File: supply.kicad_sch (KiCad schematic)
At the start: 37 parts, among them IC3 TPS259571DSGR, IC4 BQ27427YZFR, IC5 TPD6E001RSERG4, IC7 TPS62291DRVR, IC8 TPS62293DRVR, IC9 MP2722GRH-0000-Z, J4 UJ20-C-V-SMT-TR-68, J6 Conn_01x03

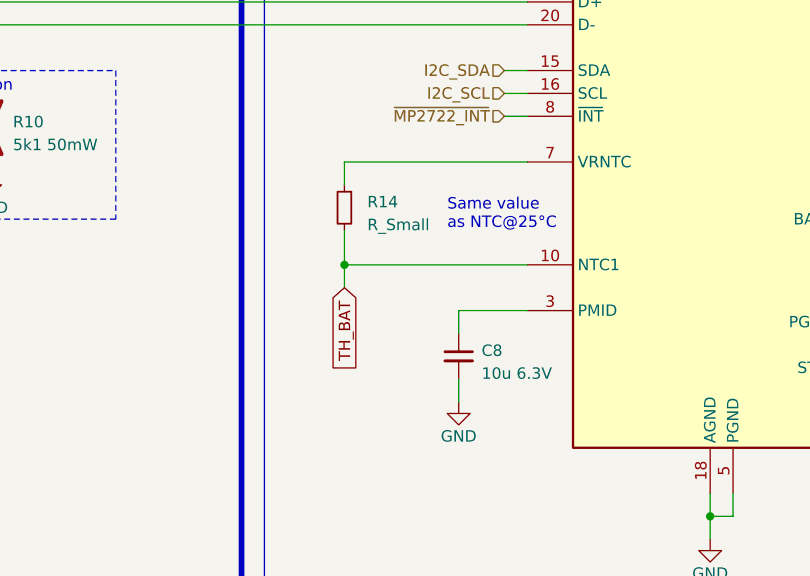
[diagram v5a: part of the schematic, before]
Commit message: added decoupling capacitors to sensors
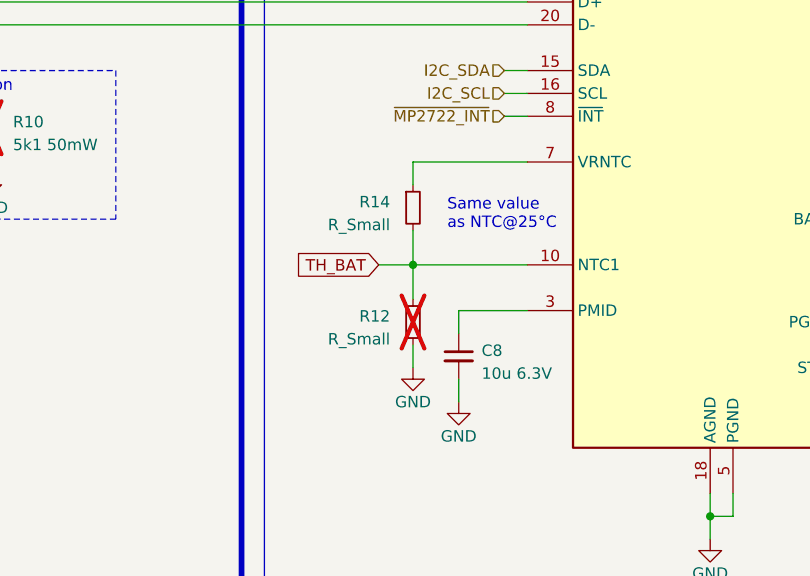
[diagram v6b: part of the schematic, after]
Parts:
- added R12: R_Small, Resistor_SMD:R_0201_0603Metric, symbol Device:R_Small
- R14: footprint (none) -> Resistor_SMD:R_0201_0603Metric
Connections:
- net EP: now also R12.2
- net TH_BAT: now also R12.1
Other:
- moved on the sheet: R14
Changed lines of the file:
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@@
   (junction (at 121.92 137.16) (diameter 0) (color 0 0 0 0)
   )
-  (junction (at 166.37 171.45) (diameter 0) (color 0 0 0 0)
+  (junction (at 173.99 171.45) (diameter 0) (color 0 0 0 0)
   )
   (junction (at 264.16 177.8) (diameter 0) (color 0 0 0 0)
@@
     (stroke (width 0) (type default))
   )
+  (wire (pts (xy 170.18 171.45) (xy 173.99 171.45))
+    (stroke (width 0) (type default))
+  )
   (wire (pts (xy 229.87 172.72) (xy 264.16 172.72))
     (stroke (width 0) (type default))
@@
     (stroke (width 0) (type default))
   )
+  (wire (pts (xy 173.99 180.34) (xy 173.99 182.88))
+    (stroke (width 0) (type default))
+  )
   (wire (pts (xy 209.55 196.85) (xy 209.55 199.39))
     (stroke (width 0) (type default))
@@
     (stroke (width 0) (type default))
   )
-  (wire (pts (xy 166.37 160.02) (xy 166.37 162.56))
+  (wire (pts (xy 173.99 160.02) (xy 173.99 162.56))
     (stroke (width 0) (type default))
   )
@@
     (stroke (width 0) (type default))
   )
-  (wire (pts (xy 166.37 167.64) (xy 166.37 171.45))
+  (wire (pts (xy 173.99 167.64) (xy 173.99 171.45))
     (stroke (width 0) (type default))
   )
@@
     (stroke (width 0) (type default))
   )
+  (wire (pts (xy 173.99 175.26) (xy 173.99 171.45))
+    (stroke (width 0) (type default))
+  )
   (wire (pts (xy 209.55 238.76) (xy 226.06 238.76))
     (stroke (width 0) (type default))
@@
     (stroke (width 0) (type default))
   )
-  (wire (pts (xy 166.37 171.45) (xy 186.69 171.45))
+  (wire (pts (xy 173.99 171.45) (xy 186.69 171.45))
     (stroke (width 0) (type default))
   )
@@
     (stroke (width 0) (type default))
   )
-  (wire (pts (xy 166.37 171.45) (xy 166.37 173.99))
-    (stroke (width 0) (type default))
-  )
   (wire (pts (xy 120.65 77.47) (xy 120.65 81.28))
     (stroke (width 0) (type default))
@@
     (stroke (width 0) (type default))
   )
-  (wire (pts (xy 166.37 160.02) (xy 186.69 160.02))
+  (wire (pts (xy 173.99 160.02) (xy 186.69 160.02))
     (stroke (width 0) (type default))
   )
@@
     )
   )
-  (global_label "TH_BAT" (shape input) (at 166.37 173.99 270) (fields_autoplaced)
+  (global_label "TH_BAT" (shape input) (at 170.18 171.45 180) (fields_autoplaced)
     (effects (font (size 1.27 1.27)) (justify right))
-    (property "Intersheetrefs" "${INTERSHEET_REFS}" (at 166.37 183.5671 90)
+    (property "Intersheetrefs" "${INTERSHEET_REFS}" (at 160.6823 171.45 0)
       (effects (font (size 1.27 1.27)) (justify right) hide)
     )
@@
   (hierarchical_label "I2C_SDA" (shape input) (at 173.99 236.22 180) (fields_autoplaced)
     (effects (font (size 1.27 1.27)) (justify right))
+  )
+  (symbol (lib_id "Device:R_Small") (at 173.99 177.8 0) (unit 1)
+    (in_bom yes) (on_board yes) (dnp yes)
+    (property "Reference" "R12" (at 171.45 177.165 0)
+      (effects (font (size 1.27 1.27)) (justify right))
+    )
+    (property "Value" "R_Small" (at 171.45 179.705 0)
+      (effects (font (size 1.27 1.27)) (justify right))
+    )
+    (property "Footprint" "Resistor_SMD:R_0201_0603Metric" (at 173.99 177.8 0)
+      (effects (font (size 1.27 1.27)) hide)
+    )
+    (property "Datasheet" "~" (at 173.99 177.8 0)
+      (effects (font (size 1.27 1.27)) hide)
+    )
+    (pin "1")
+    (pin "2")
+    (instances
+      (project "armband"
+        (path "/017c50c6-333c-4d31-ad5a-278994a09b14/ae5dc462-dca9-40e4-ba02-6b87a86a4904"
+          (reference "R12") (unit 1)
+        )
+      )
+    )
   )
   (symbol (lib_id "LibraryLoader:TPS259571DSGR") (at 193.04 35.56 0) (unit 1)
@@
         (path "/017c50c6-333c-4d31-ad5a-278994a09b14/ae5dc462-dca9-40e4-ba02-6b87a86a4904"
           (reference "J6") (unit 1)
+        )
+      )
+    )
+  )
+  (symbol (lib_id "power:GND") (at 173.99 182.88 0) (unit 1)
+    (in_bom yes) (on_board yes) (dnp no)
+    (property "Reference" "#PWR01" (at 173.99 189.23 0)
+      (effects (font (size 1.27 1.27)) hide)
+    )
+    (property "Value" "GND" (at 173.99 186.69 0)
+      (effects (font (size 1.27 1.27)))
+    )
+    (property "Footprint" "" (at 173.99 182.88 0)
+      (effects (font (size 1.27 1.27)) hide)
+    )
+    (property "Datasheet" "" (at 173.99 182.88 0)
+      (effects (font (size 1.27 1.27)) hide)
+    )
+    (pin "1")
+    (instances
+      (project "armband"
+        (path "/017c50c6-333c-4d31-ad5a-278994a09b14"
+          (reference "#PWR01") (unit 1)
+        )
+        (path "/017c50c6-333c-4d31-ad5a-278994a09b14/ae5dc462-dca9-40e4-ba02-6b87a86a4904"
+          (reference "#PWR035") (unit 1)
         )
       )
@@
     )
   )
-  (symbol (lib_id "Device:R_Small") (at 166.37 165.1 0) (mirror y) (unit 1)
-    (in_bom yes) (on_board yes) (dnp no)
-    (property "Reference" "R14" (at 168.91 164.465 0)
-      (effects (font (size 1.27 1.27)) (justify right))
-    )
-    (property "Value" "R_Small" (at 168.91 167.005 0)
-      (effects (font (size 1.27 1.27)) (justify right))
-    )
-    (property "Footprint" "" (at 166.37 165.1 0)
-      (effects (font (size 1.27 1.27)) hide)
-    )
-    (property "Datasheet" "~" (at 166.37 165.1 0)
-      (effects (font (size 1.27 1.27)) hide)
-    )
+  (symbol (lib_id "Device:R_Small") (at 173.99 165.1 0) (unit 1)
+    (in_bom yes) (on_board yes) (dnp no)
+    (property "Reference" "R14" (at 171.45 164.465 0)
+      (effects (font (size 1.27 1.27)) (justify right))
+    )
+    (property "Value" "R_Small" (at 171.45 167.005 0)
+      (effects (font (size 1.27 1.27)) (justify right))
+    )
+    (property "Footprint" "Resistor_SMD:R_0201_0603Metric" (at 173.99 165.1 0)
+      (effects (font (size 1.27 1.27)) hide)
+    )
+    (property "Datasheet" "~" (at 173.99 165.1 0)
+      (effects (font (size 1.27 1.27)) hide)
+    )

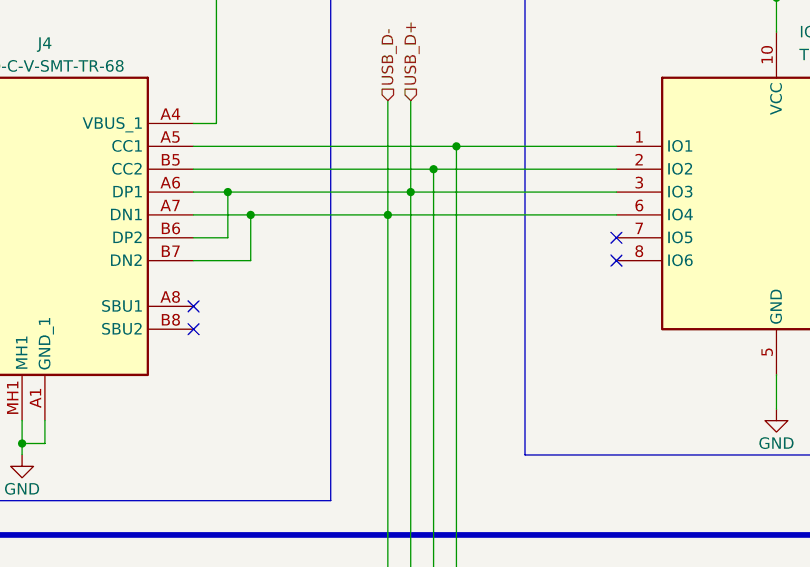
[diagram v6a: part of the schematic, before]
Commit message: added SBU pins to TVS diodes, changed button pullup resistors (QSMP)
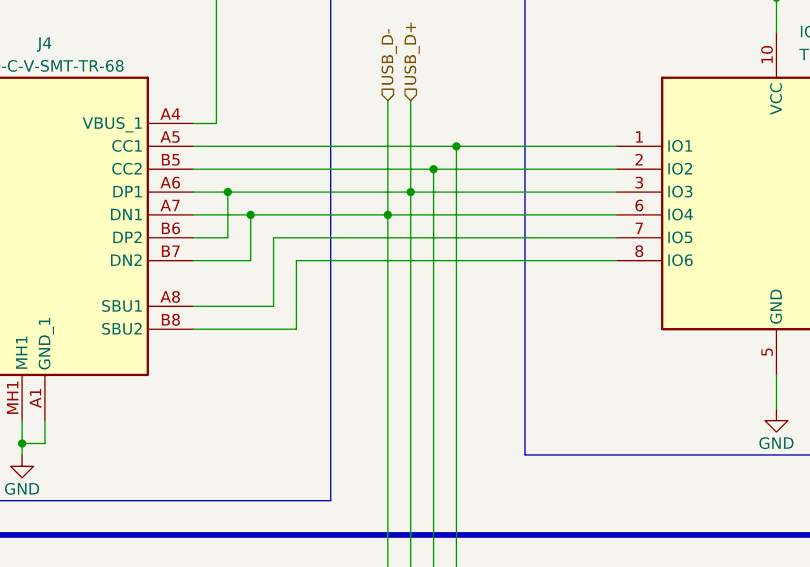
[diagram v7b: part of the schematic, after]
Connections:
- net at J4.A8 (SBU1): now also IC5.7 (IO5)
- net at J4.B8 (SBU2): now also IC5.8 (IO6)
- no-connect marks 5 -> 1
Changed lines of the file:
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@@
   (junction (at 264.16 177.8) (diameter 0) (color 0 0 0 0)
   )
-  (no_connect (at 102.87 62.23))
   (no_connect (at 232.41 190.5))
-  (no_connect (at 55.88 69.85))
-  (no_connect (at 55.88 72.39))
-  (no_connect (at 102.87 64.77))
   (wire (pts (xy 232.41 134.62) (xy 232.41 137.16))
     (stroke (width 0) (type default))
@@
     (stroke (width 0) (type default))
   )
+  (wire (pts (xy 55.88 69.85) (xy 64.77 69.85))
+    (stroke (width 0) (type default))
+  )
   (wire (pts (xy 270.51 134.62) (xy 270.51 137.16))
     (stroke (width 0) (type default))
@@
     (stroke (width 0) (type default))
   )
+  (wire (pts (xy 67.31 64.77) (xy 102.87 64.77))
+    (stroke (width 0) (type default))
+  )
   (wire (pts (xy 173.99 180.34) (xy 173.99 182.88))
     (stroke (width 0) (type default))
@@
     (stroke (width 0) (type default))
   )
+  (wire (pts (xy 55.88 72.39) (xy 67.31 72.39))
+    (stroke (width 0) (type default))
+  )
   (wire (pts (xy 82.55 54.61) (xy 82.55 139.7))
     (stroke (width 0) (type default))
@@
     (stroke (width 0) (type default))
   )
+  (wire (pts (xy 64.77 62.23) (xy 102.87 62.23))
+    (stroke (width 0) (type default))
+  )
   (wire (pts (xy 370.84 176.53) (xy 373.38 176.53))
     (stroke (width 0) (type default))
@@
     (stroke (width 0) (type default))
   )
+  (wire (pts (xy 64.77 69.85) (xy 64.77 62.23))
+    (stroke (width 0) (type default))
+  )
+  (wire (pts (xy 67.31 72.39) (xy 67.31 64.77))
+    (stroke (width 0) (type default))
+  )

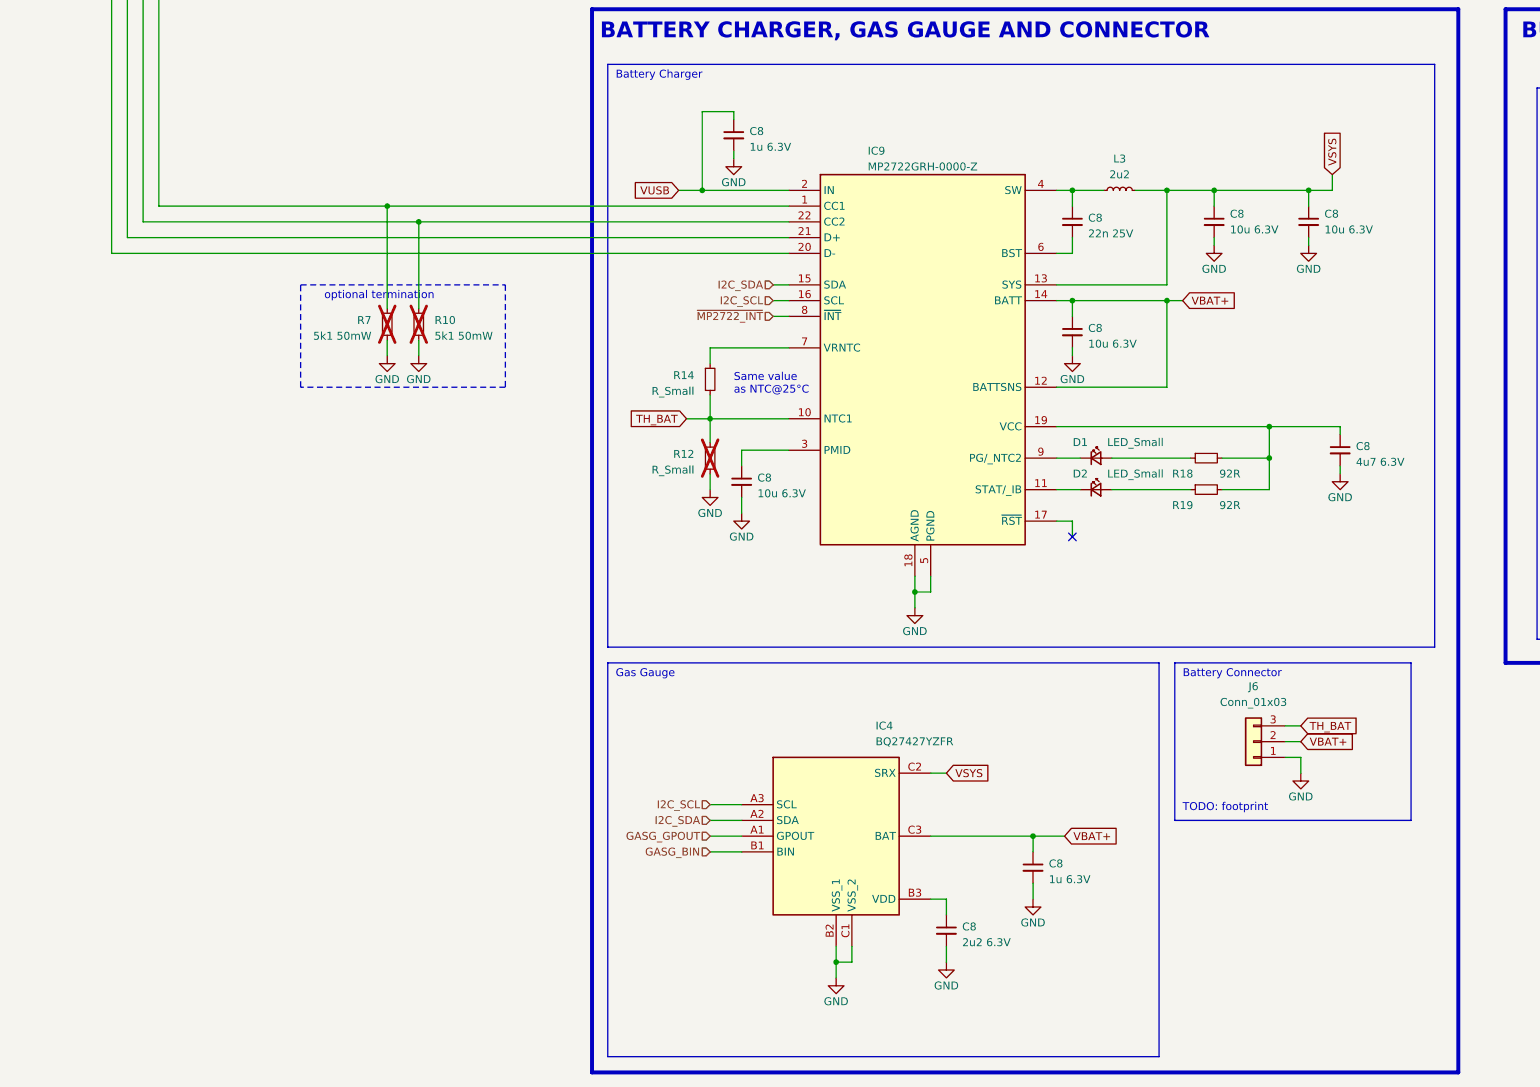
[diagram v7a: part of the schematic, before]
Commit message: added ambient light_sensor.kicad_sch
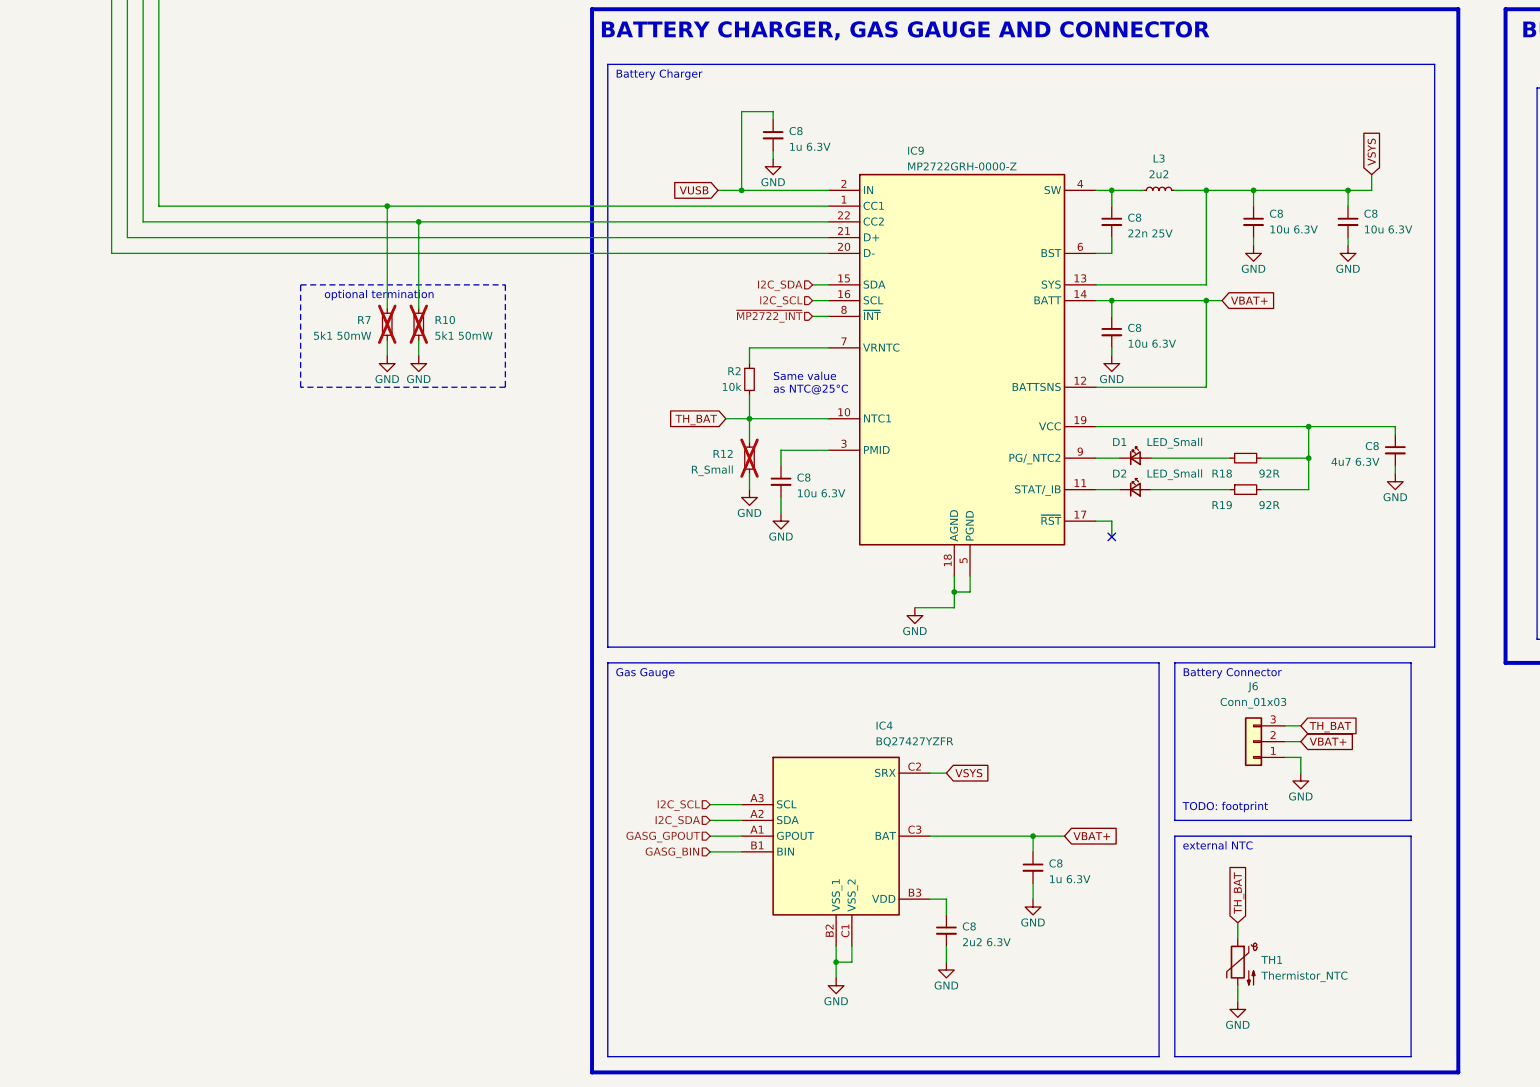
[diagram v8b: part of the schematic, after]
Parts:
- removed R14: R_Small, Resistor_SMD:R_0201_0603Metric, symbol Device:R_Small
- added R2: 10k, Resistor_SMD:R_0201_0603Metric_Pad0.64x0.40mm_HandSolder, symbol Device:R_Small
- added TH1: Thermistor_NTC, ARMband:CTTS-203856-S02, symbol Device:Thermistor_NTC
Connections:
- net EP: now also TH1.2
- net TH_BAT: now also R2.2, TH1.1
- net at IC9.7 (VRNTC): now also R2.1
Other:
- note added: "external NTC"
- moved on the sheet: C8, D1, D2, IC9, L3, R12, R18, R19
